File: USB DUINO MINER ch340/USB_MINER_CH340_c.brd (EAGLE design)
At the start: 33.7 x 25.4 mm, 17 parts, among them IC1 FT232RL, J1 USB_A_PTH_MALE, U1 ATMEGA328P_TQFP, Y1 16MHZ

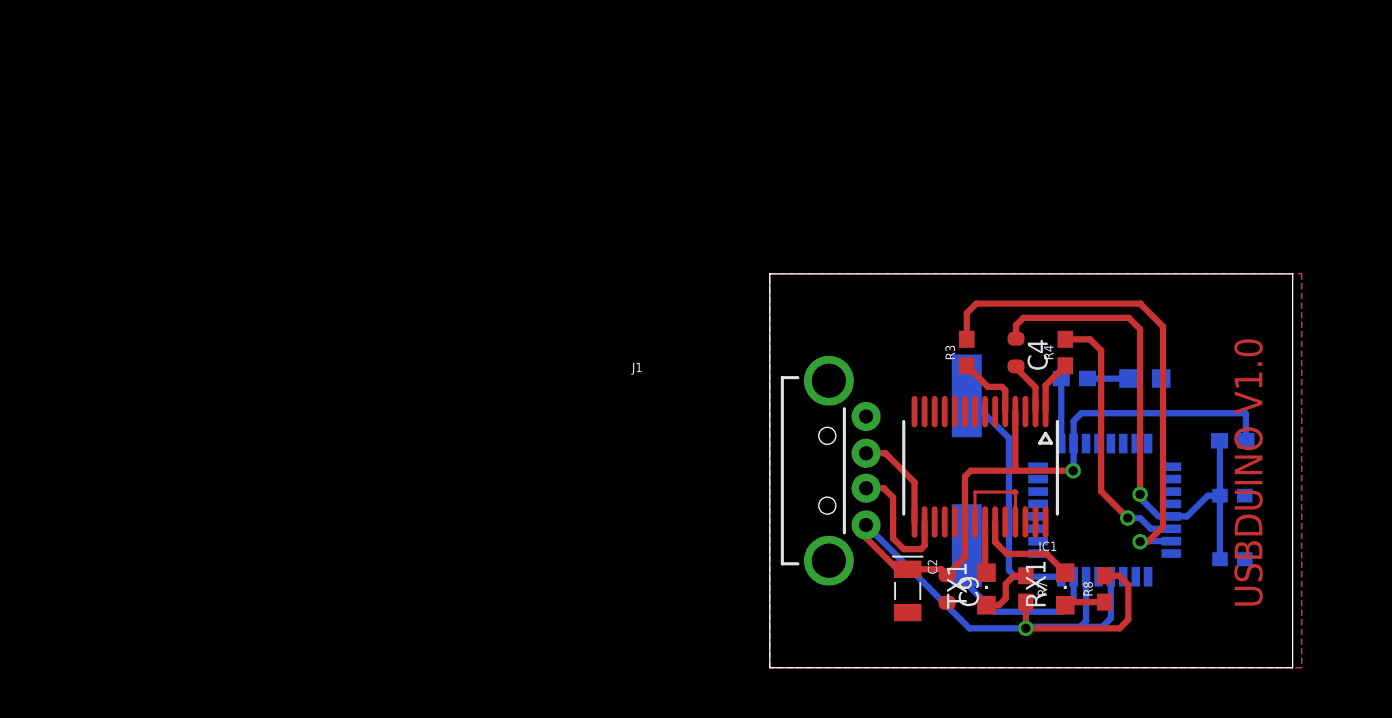
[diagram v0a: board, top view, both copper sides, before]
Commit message: Add new sketch for CH340
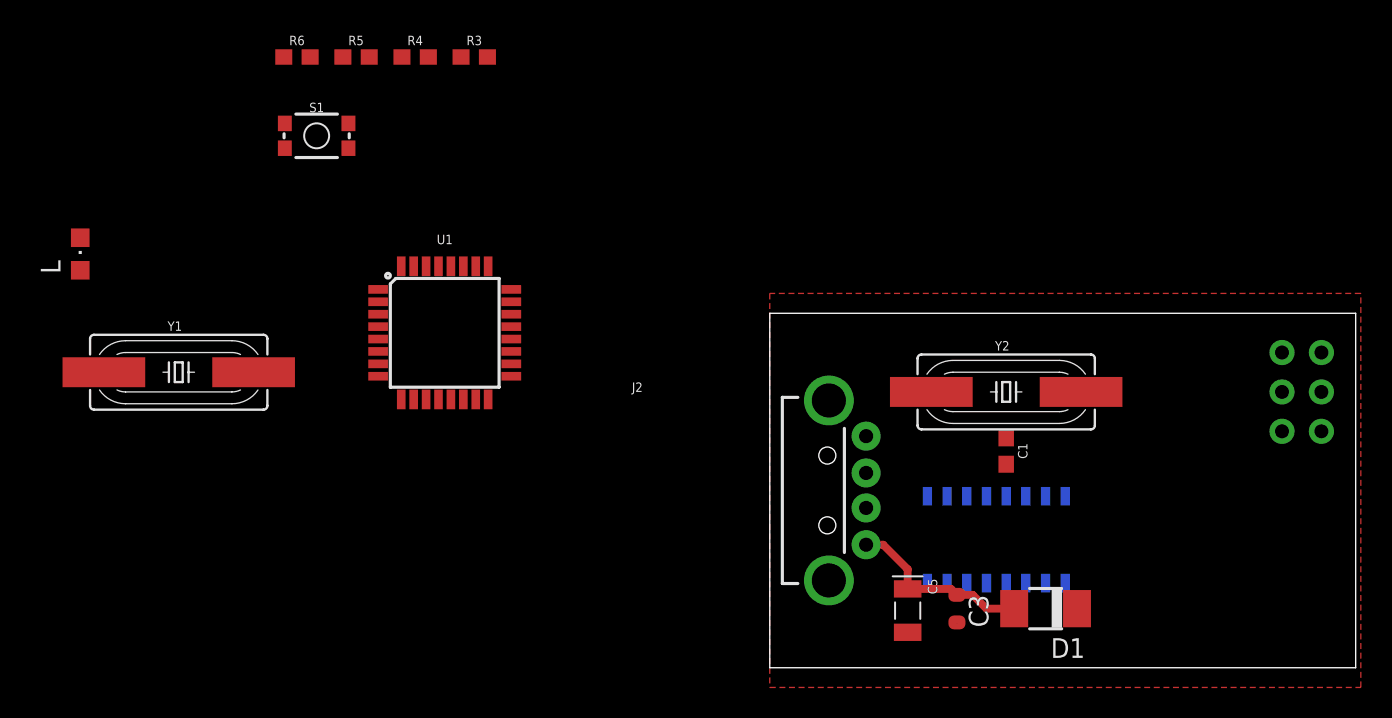
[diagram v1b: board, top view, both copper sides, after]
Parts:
- removed C2: 4,7uF_16V, Condensatori:TAN-A
- removed C4, C9: 100nF, Condensatori:C0603-ROUND
- removed IC1: FT232RL, IntegratedCircuits:SSOP28
- removed J1: USB_A_PTH_MALE, SparkFun-Connectors:USB-A-H
- removed R7, R8: 1k, SparkFun-Resistors:0603
- removed RX1: Red, Opto:CHIPLED_0805
- removed TX1: Green, Opto:CHIPLED_0805
- added C1: 100nF, SparkFun-Capacitors:0603
- added C3: 100nF, Condensatori:C0603-ROUND
- added C5: 4,7uF_16V, Condensatori:TAN-A
- added D1: SR1100, diode:DO-214AC
- added ISP1: AVRISP-6, adafruit:AVRISP
- added J2: USB_A_PTH_MALE, SparkFun-Connectors:USB-A-H
- added U2: CH340G, SparkFun-IC-Comms:SO016
- added Y2: 12MHz, SparkFun-Clocks:HC49UP
- moved L 69.1 mm to (-44.5, 26.7), flipped to the top, turned to 0 degrees
- moved R6 65.2 mm to (-30.5, 39.4), flipped to the top
- moved S1 64.2 mm to (-29.2, 34.3), flipped to the top, turned to 0 degrees
- moved Y1 51.2 mm to (-38.1, 19.1), flipped to the top, turned to 0 degrees
- moved R5 50.7 mm to (-26.7, 39.4), flipped to the top, turned to 0 degrees
- moved R4 46.0 mm to (-22.9, 39.4), turned to 0 degrees
- moved U1 44.1 mm to (-21.0, 21.6), flipped to the top, turned to 0 degrees
- moved R3 37.0 mm to (-19.1, 39.4), turned to 0 degrees
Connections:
- removed net 3V3OUT: IC1.17
- removed net N$11: R7.1, TX1.A
- removed net N$29: R8.1, RX1.A
- removed net N$4: C4.2, IC1.2
- removed net N$5: IC1.15, J1.D+
- removed net N$6: IC1.16, J1.D-
- removed net N$8: IC1.23, RX1.C
- removed net N$9: IC1.22, TX1.C
- new net D+: J2.D+, U2.5
- new net D-: J2.D-, U2.6
- new net MISO: ISP1.1
- new net MOSI: ISP1.4
- new net N$1: U2.7, Y2.2
- new net N$14: C1.2, U2.13
- new net N$2: U2.8, Y2.1
- new net SCK: ISP1.3
- new net VUSB: C3.1, C5.1, D1.A, J2.VBUS
- net +5V: now also D1.C, ISP1.2, U2.16; no longer C2.1, C9.1, IC1.20, IC1.4, J1.VBUS, R7.2, R8.2
- net COM: now also C3.2, C5.2, ISP1.6, J2.GND, J2.SHLD1, J2.SHLD2, U2.1; no longer C2.2, C9.2, IC1.18, IC1.21, IC1.25, IC1.26, IC1.7, J1.GND, J1.SHLD1, J1.SHLD2
- net RESET: now also C1.1, ISP1.5; no longer C4.1
- net RX: now also U2.2; no longer IC1.1
- net TX: now also U2.3; no longer IC1.5
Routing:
- net +5V: track 78.5 -> 0.73 mm, vias 2 -> 0
- net RESET: track 34.1 -> 0.00 mm, vias 1 -> 0
- net N$12: track 32.0 -> 0.00 mm, vias 1 -> 0
- net N$13: track 17.2 -> 0.00 mm, vias 1 -> 0
- net N$10: track 15.9 -> 0.00 mm
- net N$3: track 12.0 -> 0.00 mm
- net VUSB: track 0.00 -> 12.0 mm
- net N$6: track 8.56 -> 0.00 mm
- net N$8: track 6.63 -> 0.00 mm
- net N$5: track 6.45 -> 0.00 mm
- net COM: track 6.44 -> 0.00 mm
- net TX: track 4.51 -> 0.00 mm
- net D13/SCK: track 4.19 -> 0.00 mm
- net N$11: track 3.88 -> 0.00 mm
- net RX: track 3.49 -> 0.00 mm
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- removed copper zone on layer 16, net COM
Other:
- board size 33.7 x 25.4 mm -> 37.8 x 22.9 mm
- board text removed: "USBDUINO V1.0"
